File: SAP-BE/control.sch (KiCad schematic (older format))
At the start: 4 parts, among them U24 74LS161, U25 28C16, U26 74LS138, U27 28C16

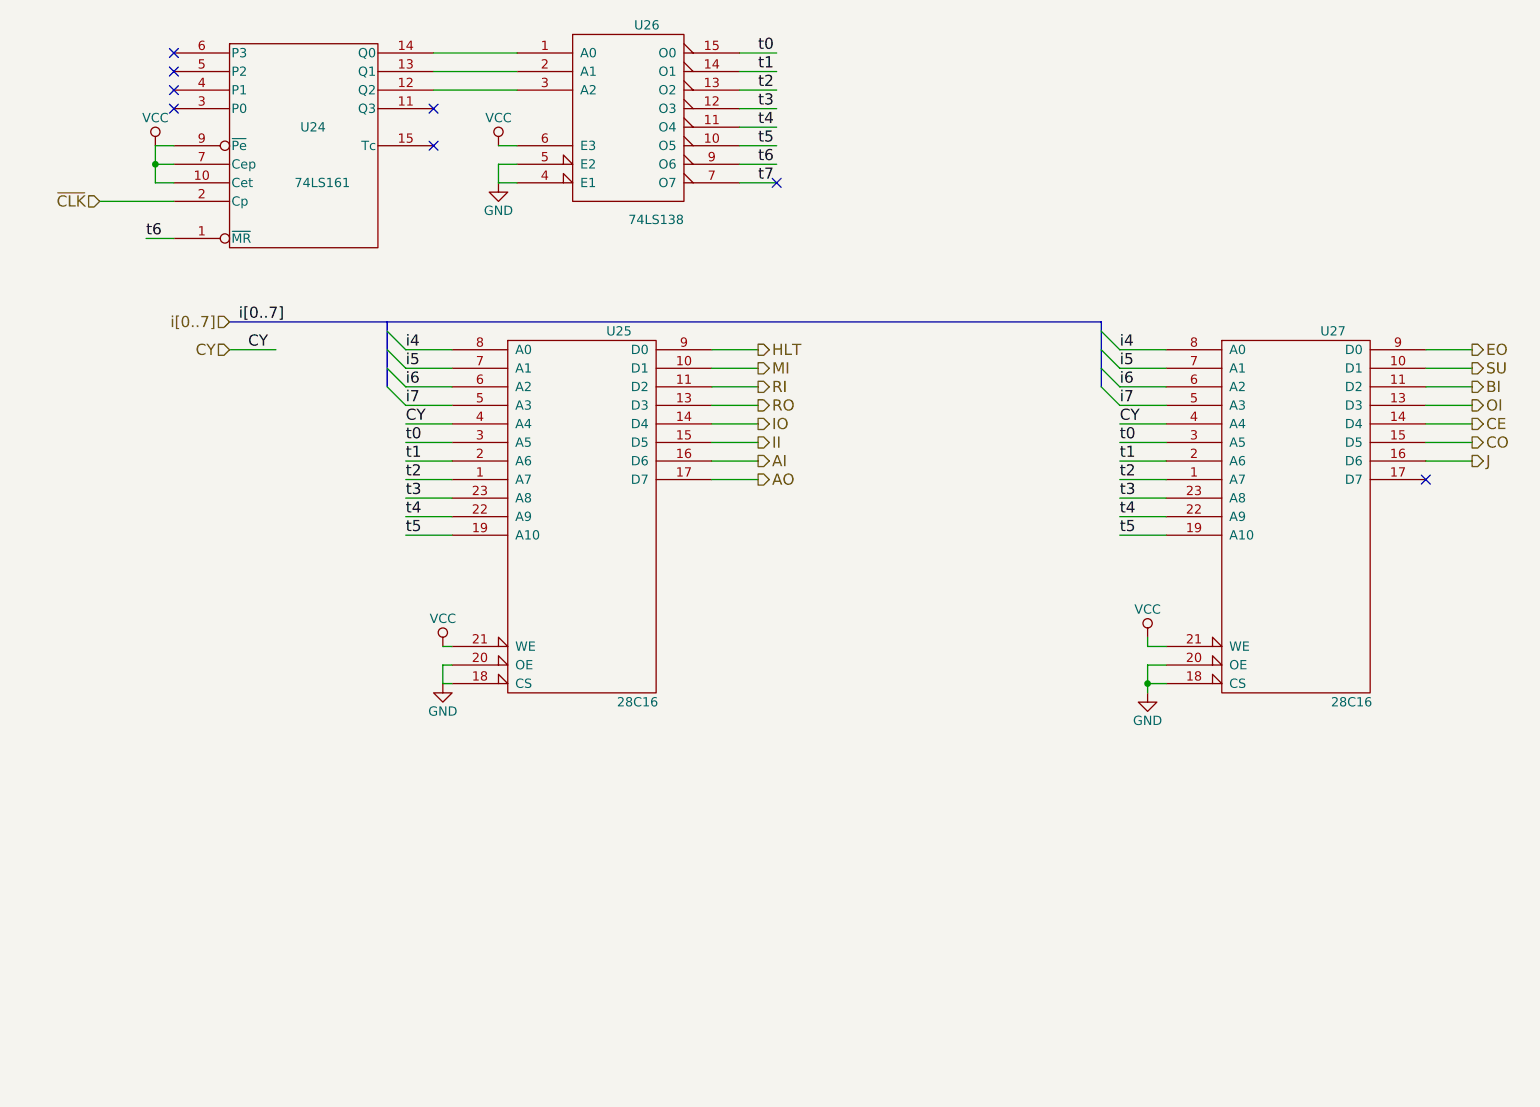
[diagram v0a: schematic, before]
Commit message: update control sheet to match video series
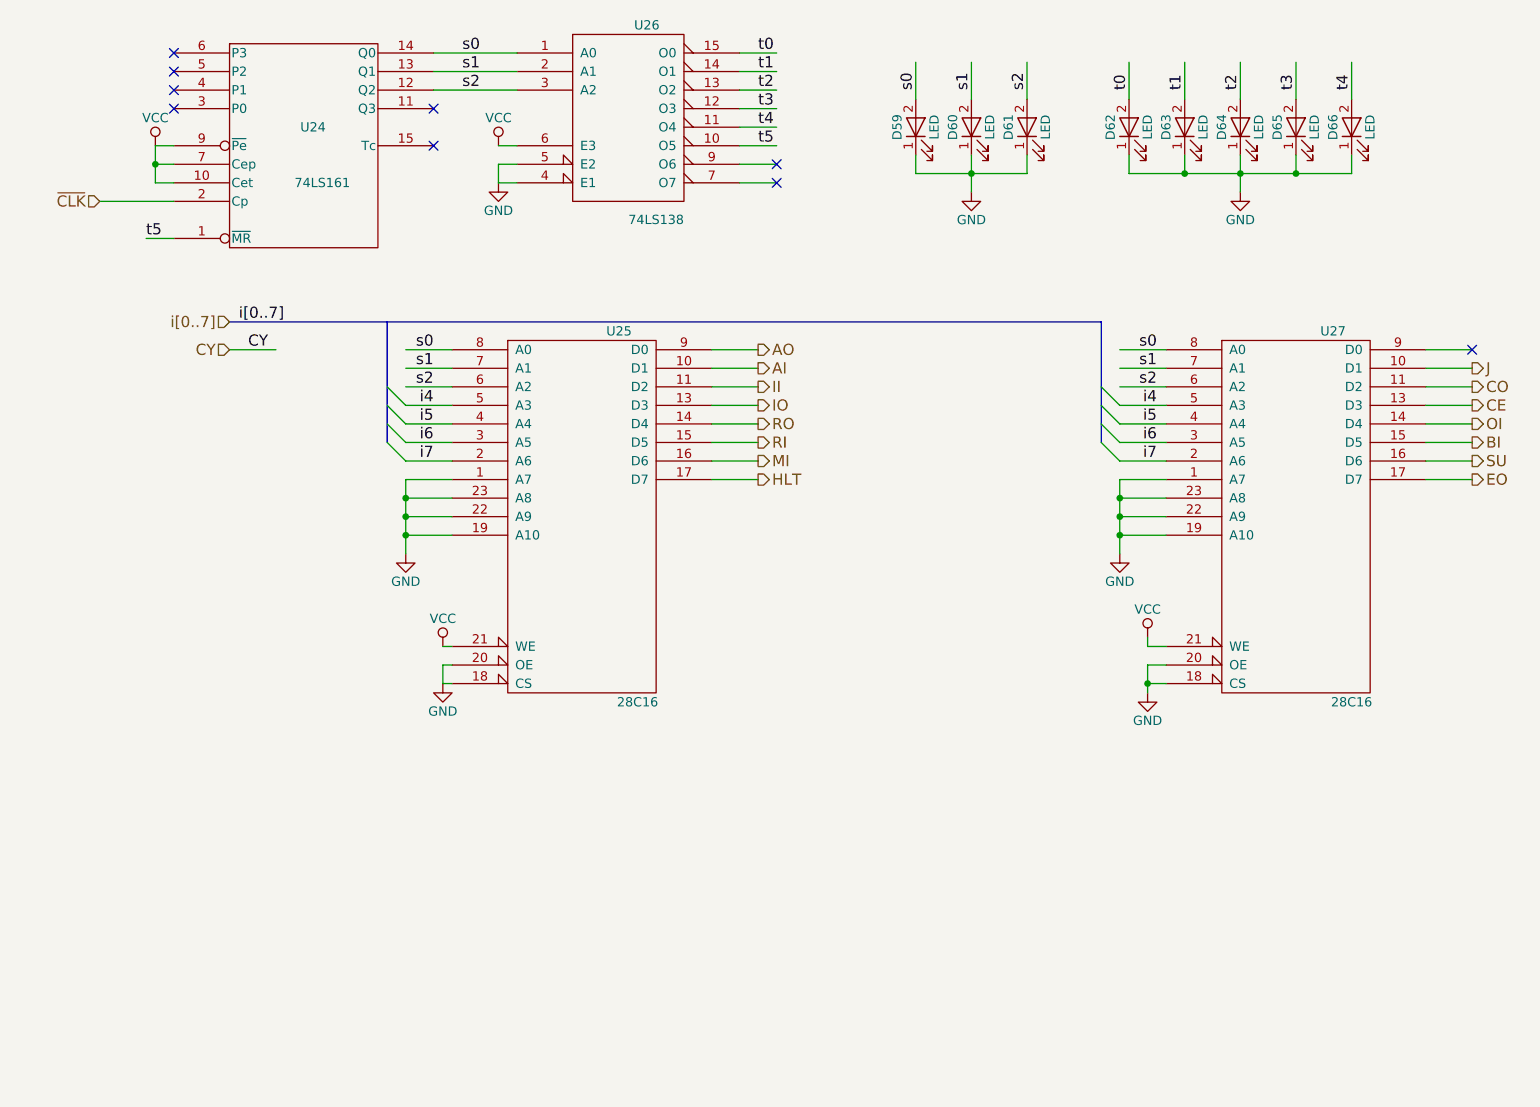
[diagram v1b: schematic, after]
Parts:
- added D59, D60, D61, D62, D63, D64, D65, D66: LED, symbol LED
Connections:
- net labels added: s0, s1, s2
- net labels removed: t6, t7
- wire segments 68 -> 89
- no-connect marks 8 -> 9

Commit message: Update with changes for reset
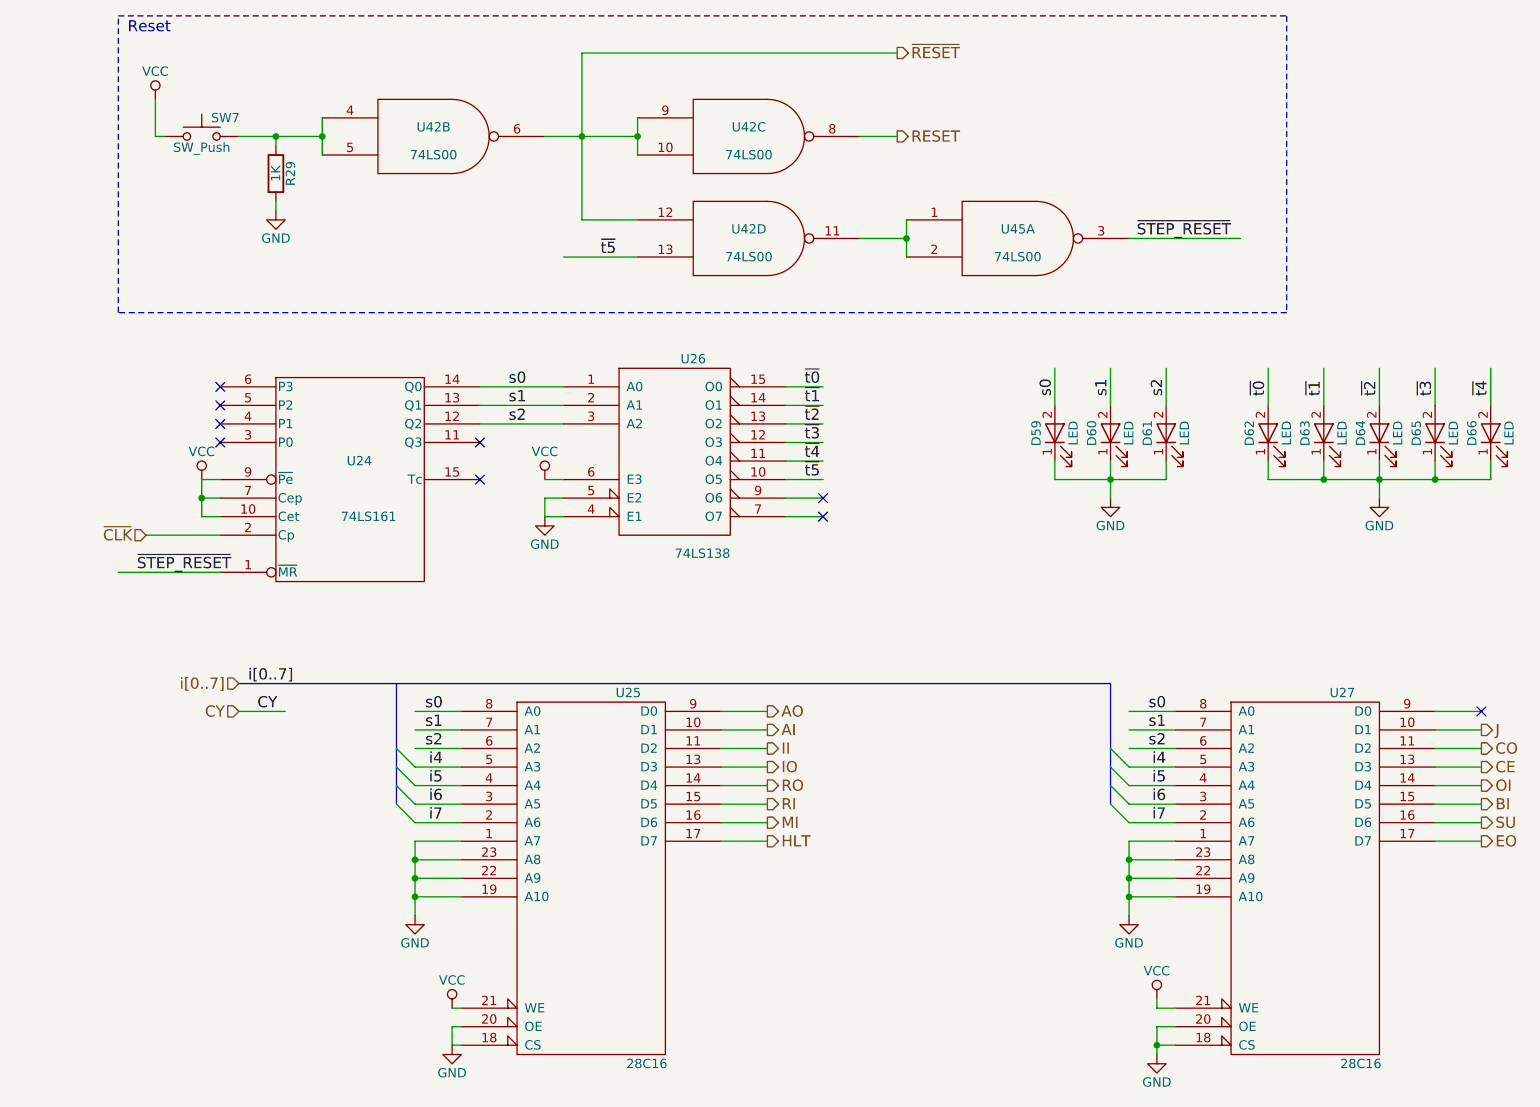
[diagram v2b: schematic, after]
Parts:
- added R29: 1K, symbol R
- added SW7: SW_Push, symbol SW_Push
- added U42, U45: 74LS00, symbol 74LS00
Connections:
- net labels added: RESET, ~RESET, ~STEP_RESET, ~t0, ~t1, ~t2, ~t3, ~t4, ~t5
- net labels removed: t0, t1, t2, t3, t4, t5
- wire segments 89 -> 105
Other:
- note added: "Reset"
- moved on the sheet: D59, D60, D61, D62, D63, D64, D65, D66, U24, U25, U26, U27

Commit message: Microcode EPROM A7 used as bank select
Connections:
- wire segments 105 -> 107

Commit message: Update with conditional flags
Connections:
- net labels added: CF, FI, ZF
- net labels removed: CY
- wire segments 107 -> 109
- no-connect marks 9 -> 8
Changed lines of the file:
@@
 $Descr A4 11693 8268
 encoding utf-8
-Sheet 9 11
+Sheet 9 12
 Title "Simple As Possible computer by Ben Eater"
 Date "2017-05-10"
@@
 Text Label 4800 3100 0    60   ~ 0
 ~t5
-Text HLabel 1750 4350 0    60   Input ~ 0
-CY
 Text HLabel 4600 5050 2    60   Output ~ 0
 HLT
@@
 i[0..7]
 Text Label 1850 4350 0    60   ~ 0
-CY
+CF
 $Comp
 L GND #PWR059
@@
 Text Label 6750 4950 2    60   ~ 0
 i7
-NoConn ~ 8450 4350
 NoConn ~ 4900 3200
 $Comp
@@
 Reset
 $Comp
-L VCC #PWR?
+L VCC #PWR069
 U 1 1 5ACBD5E7
 P 6300 5000
-F 0 "#PWR?" H 6300 4850 50  0001 C CNN
+F 0 "#PWR069" H 6300 4850 50  0001 C CNN
 F 1 "VCC" H 6300 5150 50  0000 C CNN
 F 2 "" H 6300 5000 50  0000 C CNN
@@
 	1    0    0    -1
 $EndComp
+Text HLabel 8450 4350 2    60   Output ~ 0
+FI
+Text Label 1950 4500 2    60   ~ 0
+ZF
+Text HLabel 1750 4350 0    60   Input ~ 0
+CF
+Text HLabel 1750 4500 0    60   Input ~ 0
+ZF
 Wire Wire Line
 	1650 3400 1250 3400
@@
 	2700 4950 2950 4950
 Wire Wire Line
-	2700 5050 2950 5050
+	2450 5050 2950 5050
 Wire Wire Line
 	2700 5150 2950 5150
@@
 Wire Wire Line
 	6550 5950 6550 5900
-Wire Wire Line
-	2700 5050 2700 5450
-Connection ~ 2700 5150
-Connection ~ 2700 5250
-Connection ~ 2700 5350
-Connection ~ 6550 5350
-Connection ~ 6550 5250
 Wire Wire Line
 	8450 5050 8200 5050
@@
 	1100 2200 1100 600
 Wire Wire Line
-	6550 5450 6550 5150
-Wire Wire Line
 	6300 5050 6300 5000
 Connection ~ 2700 6150
 Wire Wire Line
 	2700 5950 2700 5900
+Wire Wire Line
+	1750 4500 2000 4500
+Wire Wire Line
+	2700 5350 2700 5450
+$Comp
+L GND #PWR070
+U 1 1 5AD4813A
+P 2450 5100
+F 0 "#PWR070" H 2450 4850 50  0001 C CNN
+F 1 "GND" H 2450 4950 50  0000 C CNN
+F 2 "" H 2450 5100 50  0000 C CNN
+F 3 "" H 2450 5100 50  0000 C CNN
+	1    2450 5100
+	1    0    0    -1
+$EndComp
+Wire Wire Line
+	2450 5100 2450 5050
+Wire Wire Line
+	6550 5350 6550 5450
+Text Label 2750 5150 0    60   ~ 0
+CF
+Text Label 2750 5250 0    60   ~ 0
+ZF
+Text Label 6650 5150 0    60   ~ 0
+CF
+Text Label 6650 5250 0    60   ~ 0
+ZF
 $EndSCHEMATC
